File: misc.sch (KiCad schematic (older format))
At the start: 9 parts, among them U18 AZ1117-5.0, U19 RP117, U20 MIC5317

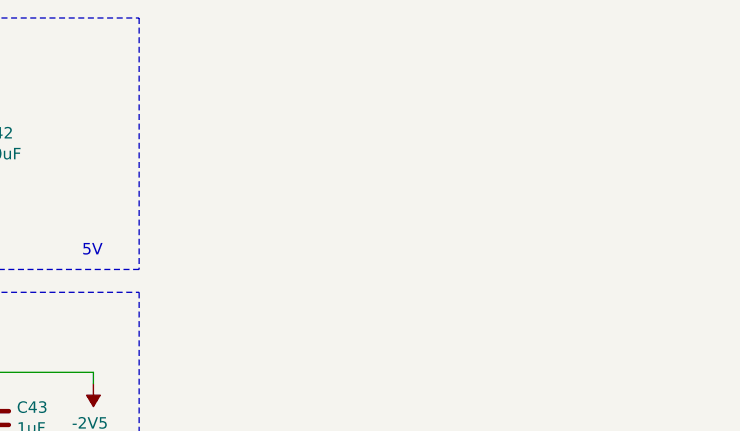
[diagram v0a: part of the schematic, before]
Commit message: Added opamp and footprints
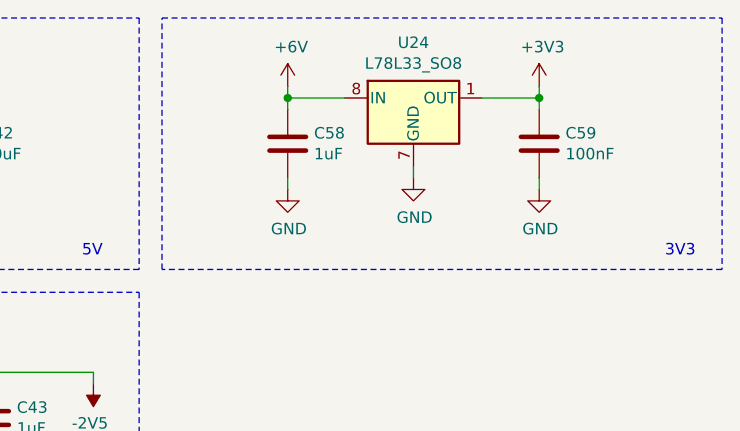
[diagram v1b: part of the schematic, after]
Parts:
- added C58: 1uF, Capacitor_SMD:C_0603_1608Metric_Pad1.08x0.95mm_HandSolder, symbol Device:C
- added C59: 100nF, Capacitor_SMD:C_0603_1608Metric_Pad1.08x0.95mm_HandSolder, symbol Device:C
- added U24: L78L33_SO8, Package_SO:SOIC-8_3.9x4.9mm_P1.27mm, symbol Regulator_Linear:L78L33_SO8
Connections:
- net +6V: now also C58.1, U24.8 (IN)
- net GND: now also C58.2, C59.2, U24.2 (GND), U24.3 (GND), U24.6 (GND), U24.7 (GND)
- new net +3V3: C59.1, U24.1 (OUT)
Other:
- note added: "3V3\n"
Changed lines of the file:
@@
 Text Notes 6850 5400 0    50   ~ 0
 2.5V
+$Comp
+L power:+6V #PWR0194
+U 1 1 6062F633
+P 7750 2300
+F 0 "#PWR0194" H 7750 2150 50  0001 C CNN
+F 1 "+6V" H 7765 2473 50  0000 C CNN
+F 2 "" H 7750 2300 50  0001 C CNN
+F 3 "" H 7750 2300 50  0001 C CNN
+	1    7750 2300
+	1    0    0    -1
+$EndComp
+Wire Wire Line
+	7750 2350 7750 2300
+$Comp
+L power:GND #PWR0195
+U 1 1 6062F63A
+P 8300 2700
+F 0 "#PWR0195" H 8300 2450 50  0001 C CNN
+F 1 "GND" H 8305 2527 50  0000 C CNN
+F 2 "" H 8300 2700 50  0001 C CNN
+F 3 "" H 8300 2700 50  0001 C CNN
+	1    8300 2700
+	1    0    0    -1
+$EndComp
+Wire Wire Line
+	8300 2650 8300 2700
+Wire Wire Line
+	8850 2350 8850 2300
+$Comp
+L Device:C C59
+U 1 1 6062F648
+P 8850 2550
+F 0 "C59" H 8965 2596 50  0000 L CNN
+F 1 "100nF" H 8965 2505 50  0000 L CNN
+F 2 "Capacitor_SMD:C_0603_1608Metric_Pad1.08x0.95mm_HandSolder" H 8888 2400 50  0001 C CNN
+F 3 "~" H 8850 2550 50  0001 C CNN
+	1    8850 2550
+	1    0    0    -1
+$EndComp
+Wire Wire Line
+	8850 2350 8850 2400
+Connection ~ 8850 2350
+$Comp
+L Device:C C58
+U 1 1 6062F650
+P 7750 2550
+F 0 "C58" H 7865 2596 50  0000 L CNN
+F 1 "1uF" H 7865 2505 50  0000 L CNN
+F 2 "Capacitor_SMD:C_0603_1608Metric_Pad1.08x0.95mm_HandSolder" H 7788 2400 50  0001 C CNN
+F 3 "~" H 7750 2550 50  0001 C CNN
+	1    7750 2550
+	1    0    0    -1
+$EndComp
+Wire Wire Line
+	7750 2350 7750 2400
+Connection ~ 7750 2350
+$Comp
+L power:GND #PWR0196
+U 1 1 6062F658
+P 7750 2750
+F 0 "#PWR0196" H 7750 2500 50  0001 C CNN
+F 1 "GND" H 7755 2577 50  0000 C CNN
+F 2 "" H 7750 2750 50  0001 C CNN
+F 3 "" H 7750 2750 50  0001 C CNN
+	1    7750 2750
+	1    0    0    -1
+$EndComp
+Wire Wire Line
+	7750 2700 7750 2750
+$Comp
+L power:GND #PWR0197
+U 1 1 6062F65F
+P 8850 2750
+F 0 "#PWR0197" H 8850 2500 50  0001 C CNN
+F 1 "GND" H 8855 2577 50  0000 C CNN
+F 2 "" H 8850 2750 50  0001 C CNN
+F 3 "" H 8850 2750 50  0001 C CNN
+	1    8850 2750
+	1    0    0    -1
+$EndComp
+Wire Wire Line
+	8850 2700 8850 2750
+Wire Wire Line
+	7750 2350 8000 2350
+Wire Wire Line
+	8600 2350 8850 2350
+Wire Notes Line
+	9650 2000 9650 3100
+Wire Notes Line
+	9650 3100 7200 3100
+Wire Notes Line
+	7200 3100 7200 2000
+Wire Notes Line
+	7200 2000 9650 2000
+Text Notes 9400 3050 0    50   ~ 0
+3V3\n
+$Comp
+L Regulator_Linear:L78L33_SO8 U24
+U 1 1 60631119
+P 8300 2350
+F 0 "U24" H 8300 2592 50  0000 C CNN
+F 1 "L78L33_SO8" H 8300 2501 50  0000 C CNN
+F 2 "Package_SO:SOIC-8_3.9x4.9mm_P1.27mm" H 8400 2550 50  0001 C CIN
+F 3 "http://www.st.com/content/ccc/resource/technical/document/datasheet/15/55/e5/aa/23/5b/43/fd/CD00000446.pdf/files/CD00000446.pdf/jcr:content/translations/en.CD00000446.pdf" H 8500 2350 50  0001 C CNN
+	1    8300 2350
+	1    0    0    -1
+$EndComp
+$Comp
+L power:+3V3 #PWR0198
+U 1 1 60631EF6
+P 8850 2300
+F 0 "#PWR0198" H 8850 2150 50  0001 C CNN
+F 1 "+3V3" H 8865 2473 50  0000 C CNN
+F 2 "" H 8850 2300 50  0001 C CNN
+F 3 "" H 8850 2300 50  0001 C CNN
+	1    8850 2300
+	1    0    0    -1
+$EndComp
 $EndSCHEMATC

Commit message: Schematic finishing touches
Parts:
- renumbered C58 to C45, C59 to C46, U24 to U21
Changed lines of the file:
@@
 $Descr A4 11693 8268
 encoding utf-8
-Sheet 4 5
+Sheet 4 6
 Title ""
 Date ""
@@
 $EndComp
 $Comp
-L power:+6V #PWR0151
+L power:+6V #PWR056
 U 1 1 6086BED5
 P 5200 2300
-F 0 "#PWR0151" H 5200 2150 50  0001 C CNN
+F 0 "#PWR056" H 5200 2150 50  0001 C CNN
 F 1 "+6V" H 5215 2473 50  0000 C CNN
 F 2 "" H 5200 2300 50  0001 C CNN
@@
 	5200 2350 5200 2300
 $Comp
-L power:GND #PWR0152
+L power:GND #PWR059
 U 1 1 6086CA4C
 P 5750 2700
-F 0 "#PWR0152" H 5750 2450 50  0001 C CNN
+F 0 "#PWR059" H 5750 2450 50  0001 C CNN
 F 1 "GND" H 5755 2527 50  0000 C CNN
 F 2 "" H 5750 2700 50  0001 C CNN
@@
 	5750 2650 5750 2700
 $Comp
-L power:+5V #PWR0153
+L power:+5V #PWR062
 U 1 1 6086D958
 P 6300 2300
-F 0 "#PWR0153" H 6300 2150 50  0001 C CNN
+F 0 "#PWR062" H 6300 2150 50  0001 C CNN
 F 1 "+5V" H 6315 2473 50  0000 C CNN
 F 2 "" H 6300 2300 50  0001 C CNN
@@
 Connection ~ 5200 2350
 $Comp
-L power:GND #PWR0154
+L power:GND #PWR057
 U 1 1 6086E5E2
 P 5200 2750
-F 0 "#PWR0154" H 5200 2500 50  0001 C CNN
+F 0 "#PWR057" H 5200 2500 50  0001 C CNN
 F 1 "GND" H 5205 2577 50  0000 C CNN
 F 2 "" H 5200 2750 50  0001 C CNN
@@
 	5200 2700 5200 2750
 $Comp
-L power:GND #PWR0155
+L power:GND #PWR063
 U 1 1 6086E8B7
 P 6300 2750
-F 0 "#PWR0155" H 6300 2500 50  0001 C CNN
+F 0 "#PWR063" H 6300 2500 50  0001 C CNN
 F 1 "GND" H 6305 2577 50  0000 C CNN
 F 2 "" H 6300 2750 50  0001 C CNN
@@
 P 6900 3600
 AR Path="/605249CC/6088BF8F" Ref="#PWR?"  Part="1"
-AR Path="/60869BAE/6088BF8F" Ref="#PWR0156"  Part="1"
-F 0 "#PWR0156" H 6900 3700 50  0001 C CNN
+AR Path="/60869BAE/6088BF8F" Ref="#PWR067"  Part="1"
+F 0 "#PWR067" H 6900 3700 50  0001 C CNN
 F 1 "-2V5" H 6915 3773 50  0000 C CNN
 F 2 "" H 6900 3600 50  0001 C CNN
@@
 P 6200 3800
 AR Path="/605249CC/6088BF95" Ref="#PWR?"  Part="1"
-AR Path="/60869BAE/6088BF95" Ref="#PWR0157"  Part="1"
-F 0 "#PWR0157" H 6200 3550 50  0001 C CNN
+AR Path="/60869BAE/6088BF95" Ref="#PWR060"  Part="1"
+F 0 "#PWR060" H 6200 3550 50  0001 C CNN
 F 1 "GND" H 6205 3627 50  0000 C CNN
 F 2 "" H 6200 3800 50  0001 C CNN
@@
 P 6450 3950
 AR Path="/605249CC/6088BFA9" Ref="#PWR?"  Part="1"
-AR Path="/60869BAE/6088BFA9" Ref="#PWR0158"  Part="1"
-F 0 "#PWR0158" H 6450 3700 50  0001 C CNN
+AR Path="/60869BAE/6088BFA9" Ref="#PWR064"  Part="1"
+F 0 "#PWR064" H 6450 3700 50  0001 C CNN
 F 1 "GND" H 6455 3777 50  0000 C CNN
 F 2 "" H 6450 3950 50  0001 C CNN
@@
 P 5050 3950
 AR Path="/605249CC/6088BFB0" Ref="#PWR?"  Part="1"
-AR Path="/60869BAE/6088BFB0" Ref="#PWR0159"  Part="1"
-F 0 "#PWR0159" H 5050 3700 50  0001 C CNN
+AR Path="/60869BAE/6088BFB0" Ref="#PWR053"  Part="1"
+F 0 "#PWR053" H 5050 3700 50  0001 C CNN
 F 1 "GND" H 5055 3777 50  0000 C CNN
 F 2 "" H 5050 3950 50  0001 C CNN
@@
 P 4800 3650
 AR Path="/605249CC/6088BFBA" Ref="#PWR?"  Part="1"
-AR Path="/60869BAE/6088BFBA" Ref="#PWR0160"  Part="1"
-F 0 "#PWR0160" H 4800 3750 50  0001 C CNN
+AR Path="/60869BAE/6088BFBA" Ref="#PWR052"  Part="1"
+F 0 "#PWR052" H 4800 3750 50  0001 C CNN
 F 1 "-5V" H 4815 3823 50  0000 C CNN
 F 2 "" H 4800 3650 50  0001 C CNN
@@
 P 5400 3700
 AR Path="/605249CC/6088BFC1" Ref="#PWR?"  Part="1"
-AR Path="/60869BAE/6088BFC1" Ref="#PWR0161"  Part="1"
-F 0 "#PWR0161" H 5400 3550 50  0001 C CNN
+AR Path="/60869BAE/6088BFC1" Ref="#PWR058"  Part="1"
+F 0 "#PWR058" H 5400 3550 50  0001 C CNN
 F 1 "+6V" H 5300 3800 50  0000 C CNN
 F 2 "" H 5400 3700 50  0001 C CNN
@@
 P 5050 4700
 AR Path="/605249CC/6088BFCF" Ref="#PWR?"  Part="1"
-AR Path="/60869BAE/6088BFCF" Ref="#PWR0162"  Part="1"
-F 0 "#PWR0162" H 5050 4550 50  0001 C CNN
+AR Path="/60869BAE/6088BFCF" Ref="#PWR054"  Part="1"
+F 0 "#PWR054" H 5050 4550 50  0001 C CNN
 F 1 "+6V" H 4950 4800 50  0000 C CNN
 F 2 "" H 5050 4700 50  0001 C CNN
@@
 P 6450 4700
 AR Path="/605249CC/6088BFD5" Ref="#PWR?"  Part="1"
-AR Path="/60869BAE/6088BFD5" Ref="#PWR0163"  Part="1"
-F 0 "#PWR0163" H 6450 4550 50  0001 C CNN
+AR Path="/60869BAE/6088BFD5" Ref="#PWR065"  Part="1"
+F 0 "#PWR065" H 6450 4550 50  0001 C CNN
 F 1 "+2V5" H 6465 4873 50  0000 C CNN
 F 2 "" H 6450 4700 50  0001 C CNN
@@
 P 6200 5000
 AR Path="/605249CC/6088BFDB" Ref="#PWR?"  Part="1"
-AR Path="/60869BAE/6088BFDB" Ref="#PWR0164"  Part="1"
-F 0 "#PWR0164" H 6200 4750 50  0001 C CNN
+AR Path="/60869BAE/6088BFDB" Ref="#PWR061"  Part="1"
+F 0 "#PWR061" H 6200 4750 50  0001 C CNN
 F 1 "GND" H 6205 4827 50  0000 C CNN
 F 2 "" H 6200 5000 50  0001 C CNN
@@
 P 5050 5150
 AR Path="/605249CC/6088BFF0" Ref="#PWR?"  Part="1"
-AR Path="/60869BAE/6088BFF0" Ref="#PWR0165"  Part="1"
-F 0 "#PWR0165" H 5050 4900 50  0001 C CNN
+AR Path="/60869BAE/6088BFF0" Ref="#PWR055"  Part="1"
+F 0 "#PWR055" H 5050 4900 50  0001 C CNN
 F 1 "GND" H 5055 4977 50  0000 C CNN
 F 2 "" H 5050 5150 50  0001 C CNN
@@
 P 6450 5150
 AR Path="/605249CC/6088BFFF" Ref="#PWR?"  Part="1"
-AR Path="/60869BAE/6088BFFF" Ref="#PWR0166"  Part="1"
-F 0 "#PWR0166" H 6450 4900 50  0001 C CNN
+AR Path="/60869BAE/6088BFFF" Ref="#PWR066"  Part="1"
+F 0 "#PWR066" H 6450 4900 50  0001 C CNN
 F 1 "GND" H 6455 4977 50  0000 C CNN
 F 2 "" H 6450 5150 50  0001 C CNN
@@
 2.5V
 $Comp
-L power:+6V #PWR0194
+L power:+6V #PWR068
 U 1 1 6062F633
 P 7750 2300
-F 0 "#PWR0194" H 7750 2150 50  0001 C CNN
+F 0 "#PWR068" H 7750 2150 50  0001 C CNN
 F 1 "+6V" H 7765 2473 50  0000 C CNN
 F 2 "" H 7750 2300 50  0001 C CNN
@@
 	7750 2350 7750 2300
 $Comp
-L power:GND #PWR0195
+L power:GND #PWR070
 U 1 1 6062F63A
 P 8300 2700
-F 0 "#PWR0195" H 8300 2450 50  0001 C CNN
+F 0 "#PWR070" H 8300 2450 50  0001 C CNN
 F 1 "GND" H 8305 2527 50  0000 C CNN
 F 2 "" H 8300 2700 50  0001 C CNN
@@
 	8850 2350 8850 2300
 $Comp
-L Device:C C59
+L Device:C C46
 U 1 1 6062F648
 P 8850 2550
-F 0 "C59" H 8965 2596 50  0000 L CNN
+F 0 "C46" H 8965 2596 50  0000 L CNN
 F 1 "100nF" H 8965 2505 50  0000 L CNN
 F 2 "Capacitor_SMD:C_0603_1608Metric_Pad1.08x0.95mm_HandSolder" H 8888 2400 50  0001 C CNN
@@
 Connection ~ 8850 2350
 $Comp
-L Device:C C58
+L Device:C C45
 U 1 1 6062F650
 P 7750 2550
-F 0 "C58" H 7865 2596 50  0000 L CNN
+F 0 "C45" H 7865 2596 50  0000 L CNN
 F 1 "1uF" H 7865 2505 50  0000 L CNN
 F 2 "Capacitor_SMD:C_0603_1608Metric_Pad1.08x0.95mm_HandSolder" H 7788 2400 50  0001 C CNN
@@
 Connection ~ 7750 2350
 $Comp
-L power:GND #PWR0196
+L power:GND #PWR069
 U 1 1 6062F658
 P 7750 2750
-F 0 "#PWR0196" H 7750 2500 50  0001 C CNN
+F 0 "#PWR069" H 7750 2500 50  0001 C CNN
 F 1 "GND" H 7755 2577 50  0000 C CNN
 F 2 "" H 7750 2750 50  0001 C CNN
@@
 	7750 2700 7750 2750
 $Comp
-L power:GND #PWR0197
+L power:GND #PWR072
 U 1 1 6062F65F
 P 8850 2750
-F 0 "#PWR0197" H 8850 2500 50  0001 C CNN
+F 0 "#PWR072" H 8850 2500 50  0001 C CNN
 F 1 "GND" H 8855 2577 50  0000 C CNN
 F 2 "" H 8850 2750 50  0001 C CNN
@@
 3V3\n
 $Comp
-L Regulator_Linear:L78L33_SO8 U24
+L Regulator_Linear:L78L33_SO8 U21
 U 1 1 60631119
 P 8300 2350
-F 0 "U24" H 8300 2592 50  0000 C CNN
+F 0 "U21" H 8300 2592 50  0000 C CNN
 F 1 "L78L33_SO8" H 8300 2501 50  0000 C CNN
 F 2 "Package_SO:SOIC-8_3.9x4.9mm_P1.27mm" H 8400 2550 50  0001 C CIN
@@
 $EndComp
 $Comp
-L power:+3V3 #PWR0198
+L power:+3V3 #PWR071
 U 1 1 60631EF6
 P 8850 2300
-F 0 "#PWR0198" H 8850 2150 50  0001 C CNN
+F 0 "#PWR071" H 8850 2150 50  0001 C CNN
 F 1 "+3V3" H 8865 2473 50  0000 C CNN
 F 2 "" H 8850 2300 50  0001 C CNN

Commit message: -2.5V regulator footprint added. RF switch footprint created and added.
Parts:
- U19: footprint (none) -> Package_TO_SOT_SMD:SOT-353_SC-70-5_Handsoldering
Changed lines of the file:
@@
 F 0 "U19" H 5800 4015 50  0000 C CNN
 F 1 "RP117" H 5800 3924 50  0000 C CNN
-F 2 "" H 5800 3650 50  0001 C CNN
+F 2 "Package_TO_SOT_SMD:SOT-353_SC-70-5_Handsoldering" H 5800 3650 50  0001 C CNN
 F 3 "" H 5800 3650 50  0001 C CNN
 	1    5800 3650

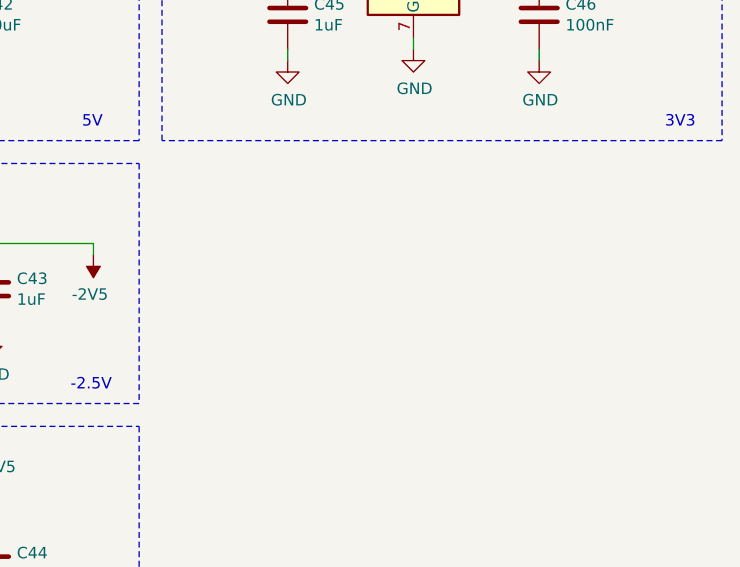
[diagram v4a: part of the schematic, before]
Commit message: IF and power layout mostly finished
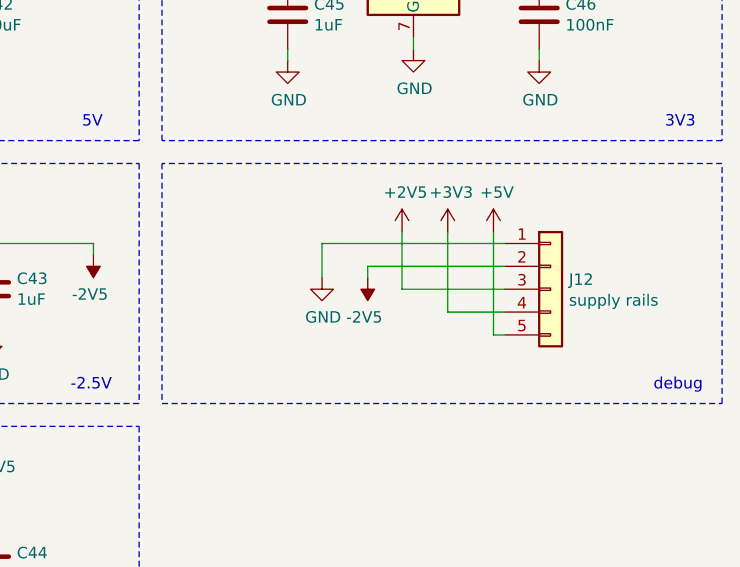
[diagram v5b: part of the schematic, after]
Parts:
- added J12: supply rails, Connector_PinHeader_2.54mm:PinHeader_1x05_P2.54mm_Vertical, symbol Connector_Generic:Conn_01x05
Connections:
- net +2V5: now also J12.3 (Pin_3)
- net +3V3: now also J12.4 (Pin_4)
- net +5V: now also J12.5 (Pin_5)
- net -2V5: now also J12.2 (Pin_2)
- net GND: now also J12.1 (Pin_1)
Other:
- note added: "debug"

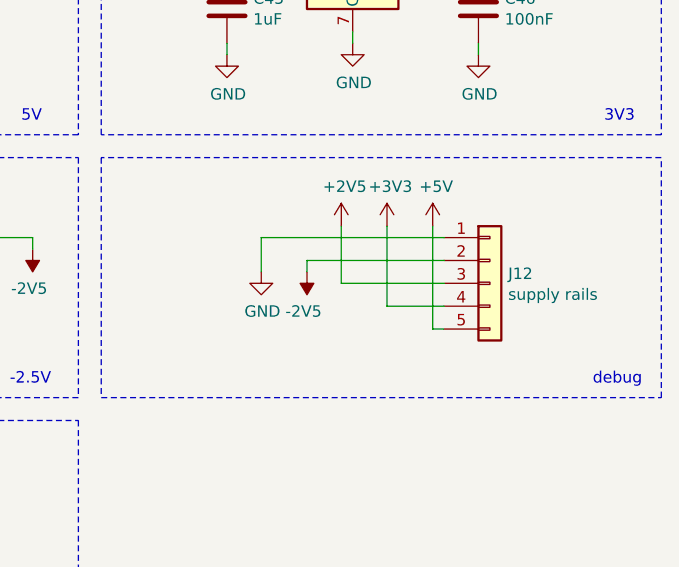
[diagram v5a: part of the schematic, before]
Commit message: Added RX shield
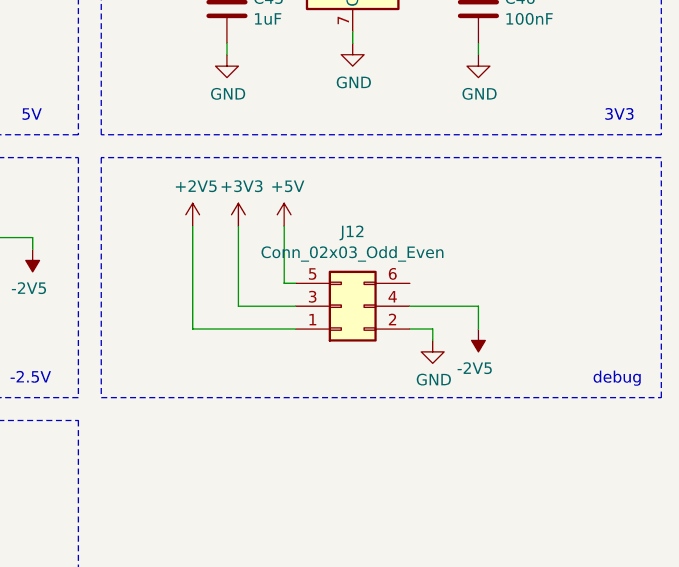
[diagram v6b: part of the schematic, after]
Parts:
- removed J12: supply rails, Connector_PinHeader_2.54mm:PinHeader_1x05_P2.54mm_Vertical, symbol Connector_Generic:Conn_01x05
- added J12: Conn_02x03_Odd_Even, Connector_PinHeader_2.54mm:PinHeader_2x03_P2.54mm_Vertical, symbol Connector_Generic:Conn_02x03_Odd_Even
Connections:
- net +2V5: now also J12.1 (Pin_1)
- net +3V3: now also J12.3 (Pin_3)
- net +5V: now also J12.5 (Pin_5)
- net -2V5: now also J12.4 (Pin_4)
- net GND: now also J12.2 (Pin_2)
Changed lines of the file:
@@
-$EndComp
-$Comp
-L Connector_Generic:Conn_01x05 J12
-U 1 1 607A9003
-P 8900 3750
-F 0 "J12" H 8980 3792 50  0000 L CNN
-F 1 "supply rails" H 8980 3701 50  0000 L CNN
-F 2 "Connector_PinHeader_2.54mm:PinHeader_1x05_P2.54mm_Vertical" H 8900 3750 50  0001 C CNN
-F 3 "~" H 8900 3750 50  0001 C CNN
-	1    8900 3750
-	1    0    0    -1
 $EndComp
 $Comp
@@
 L power:-2V5 #PWR?
 U 1 1 607AEF68
-P 8100 3700
+P 8850 3950
 AR Path="/605249CC/607AEF68" Ref="#PWR?"  Part="1"
 AR Path="/60869BAE/607AEF68" Ref="#PWR075"  Part="1"
-F 0 "#PWR075" H 8100 3800 50  0001 C CNN
-F 1 "-2V5" H 8115 3873 50  0000 C CNN
-F 2 "" H 8100 3700 50  0001 C CNN
-F 3 "" H 8100 3700 50  0001 C CNN
-	1    8100 3700
+F 0 "#PWR075" H 8850 4050 50  0001 C CNN
+F 1 "-2V5" H 8865 4123 50  0000 C CNN
+F 2 "" H 8850 3950 50  0001 C CNN
+F 3 "" H 8850 3950 50  0001 C CNN
+	1    8850 3950
 	-1   0    0    1
 $EndComp
@@
 L power:+2V5 #PWR?
 U 1 1 607AF678
-P 8250 3500
+P 7600 3500
 AR Path="/605249CC/607AF678" Ref="#PWR?"  Part="1"
 AR Path="/60869BAE/607AF678" Ref="#PWR076"  Part="1"
-F 0 "#PWR076" H 8250 3350 50  0001 C CNN
-F 1 "+2V5" H 8265 3673 50  0000 C CNN
-F 2 "" H 8250 3500 50  0001 C CNN
-F 3 "" H 8250 3500 50  0001 C CNN
-	1    8250 3500
+F 0 "#PWR076" H 7600 3350 50  0001 C CNN
+F 1 "+2V5" H 7615 3673 50  0000 C CNN
+F 2 "" H 7600 3500 50  0001 C CNN
+F 3 "" H 7600 3500 50  0001 C CNN
+	1    7600 3500
 	1    0    0    -1
 $EndComp
@@
 L power:GND #PWR074
 U 1 1 607AFAD5
-P 7900 3700
-F 0 "#PWR074" H 7900 3450 50  0001 C CNN
-F 1 "GND" H 7905 3527 50  0000 C CNN
-F 2 "" H 7900 3700 50  0001 C CNN
-F 3 "" H 7900 3700 50  0001 C CNN
-	1    7900 3700
-	1    0    0    -1
-$EndComp
-$Comp
-L power:+5V #PWR078
-U 1 1 607AFDF0
-P 8650 3500
-F 0 "#PWR078" H 8650 3350 50  0001 C CNN
-F 1 "+5V" H 8665 3673 50  0000 C CNN
-F 2 "" H 8650 3500 50  0001 C CNN
-F 3 "" H 8650 3500 50  0001 C CNN
-	1    8650 3500
+P 8650 4000
+F 0 "#PWR074" H 8650 3750 50  0001 C CNN
+F 1 "GND" H 8655 3827 50  0000 C CNN
+F 2 "" H 8650 4000 50  0001 C CNN
+F 3 "" H 8650 4000 50  0001 C CNN
+	1    8650 4000
 	1    0    0    -1
 $EndComp
@@
 L power:+3V3 #PWR077
 U 1 1 607BC223
-P 8450 3500
-F 0 "#PWR077" H 8450 3350 50  0001 C CNN
-F 1 "+3V3" H 8465 3673 50  0000 C CNN
-F 2 "" H 8450 3500 50  0001 C CNN
-F 3 "" H 8450 3500 50  0001 C CNN
-	1    8450 3500
+P 7800 3500
+F 0 "#PWR077" H 7800 3350 50  0001 C CNN
+F 1 "+3V3" H 7815 3673 50  0000 C CNN
+F 2 "" H 7800 3500 50  0001 C CNN
+F 3 "" H 7800 3500 50  0001 C CNN
+	1    7800 3500
 	1    0    0    -1
 $EndComp
-Wire Wire Line
-	8250 3500 8250 3750
-Wire Wire Line
-	8250 3750 8700 3750
-Wire Wire Line
-	8450 3500 8450 3850
-Wire Wire Line
-	8450 3850 8700 3850
-Wire Wire Line
-	8650 3500 8650 3950
-Wire Wire Line
-	8650 3950 8700 3950
-Wire Wire Line
-	8700 3550 7900 3550
-Wire Wire Line
-	7900 3550 7900 3700
-Wire Wire Line
-	8700 3650 8100 3650
-Wire Wire Line
-	8100 3650 8100 3700
 Wire Notes Line
 	7200 3200 7200 4250
@@
 Text Notes 9350 4200 0    50   ~ 0
 debug
+$Comp
+L Connector_Generic:Conn_02x03_Odd_Even J12
+U 1 1 60750802
+P 8250 3850
+F 0 "J12" H 8300 3525 50  0000 C CNN
+F 1 "Conn_02x03_Odd_Even" H 8300 3616 50  0000 C CNN
+F 2 "Connector_PinHeader_2.54mm:PinHeader_2x03_P2.54mm_Vertical" H 8250 3850 50  0001 C CNN
+F 3 "~" H 8250 3850 50  0001 C CNN
+	1    8250 3850
+	1    0    0    1
+$EndComp
+$Comp
+L power:+5V #PWR078
+U 1 1 607AFDF0
+P 8000 3500
+F 0 "#PWR078" H 8000 3350 50  0001 C CNN
+F 1 "+5V" H 8015 3673 50  0000 C CNN
+F 2 "" H 8000 3500 50  0001 C CNN
+F 3 "" H 8000 3500 50  0001 C CNN
+	1    8000 3500
+	1    0    0    -1
+$EndComp
+Wire Wire Line
+	8000 3500 8000 3750
+Wire Wire Line
+	8000 3750 8050 3750
+Wire Wire Line
+	8050 3850 7800 3850
+Wire Wire Line
+	7800 3850 7800 3500
+Wire Wire Line
+	7600 3950 8050 3950
+Wire Wire Line
+	7600 3500 7600 3950
+Wire Wire Line
+	8550 3950 8650 3950
+Wire Wire Line
+	8650 3950 8650 4000
+Wire Wire Line
+	8550 3850 8850 3850
+Wire Wire Line
+	8850 3850 8850 3950
 $EndSCHEMATC
